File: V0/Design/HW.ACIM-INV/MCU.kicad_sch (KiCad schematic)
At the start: 86 parts, among them J2 ICSP, J5 PSU ICSP, J6 INV DEBUG, J8 ENCODER, Q2 20V/1A, Q3 20V/1A, Q7 20V/1A, SW1 PRG SEL, U11 256Kbit EEPROM, U13 128Mbit Flash, U5 MIPS 32-bit DSC, U6 12MHz (3225), X1 32.768kHz

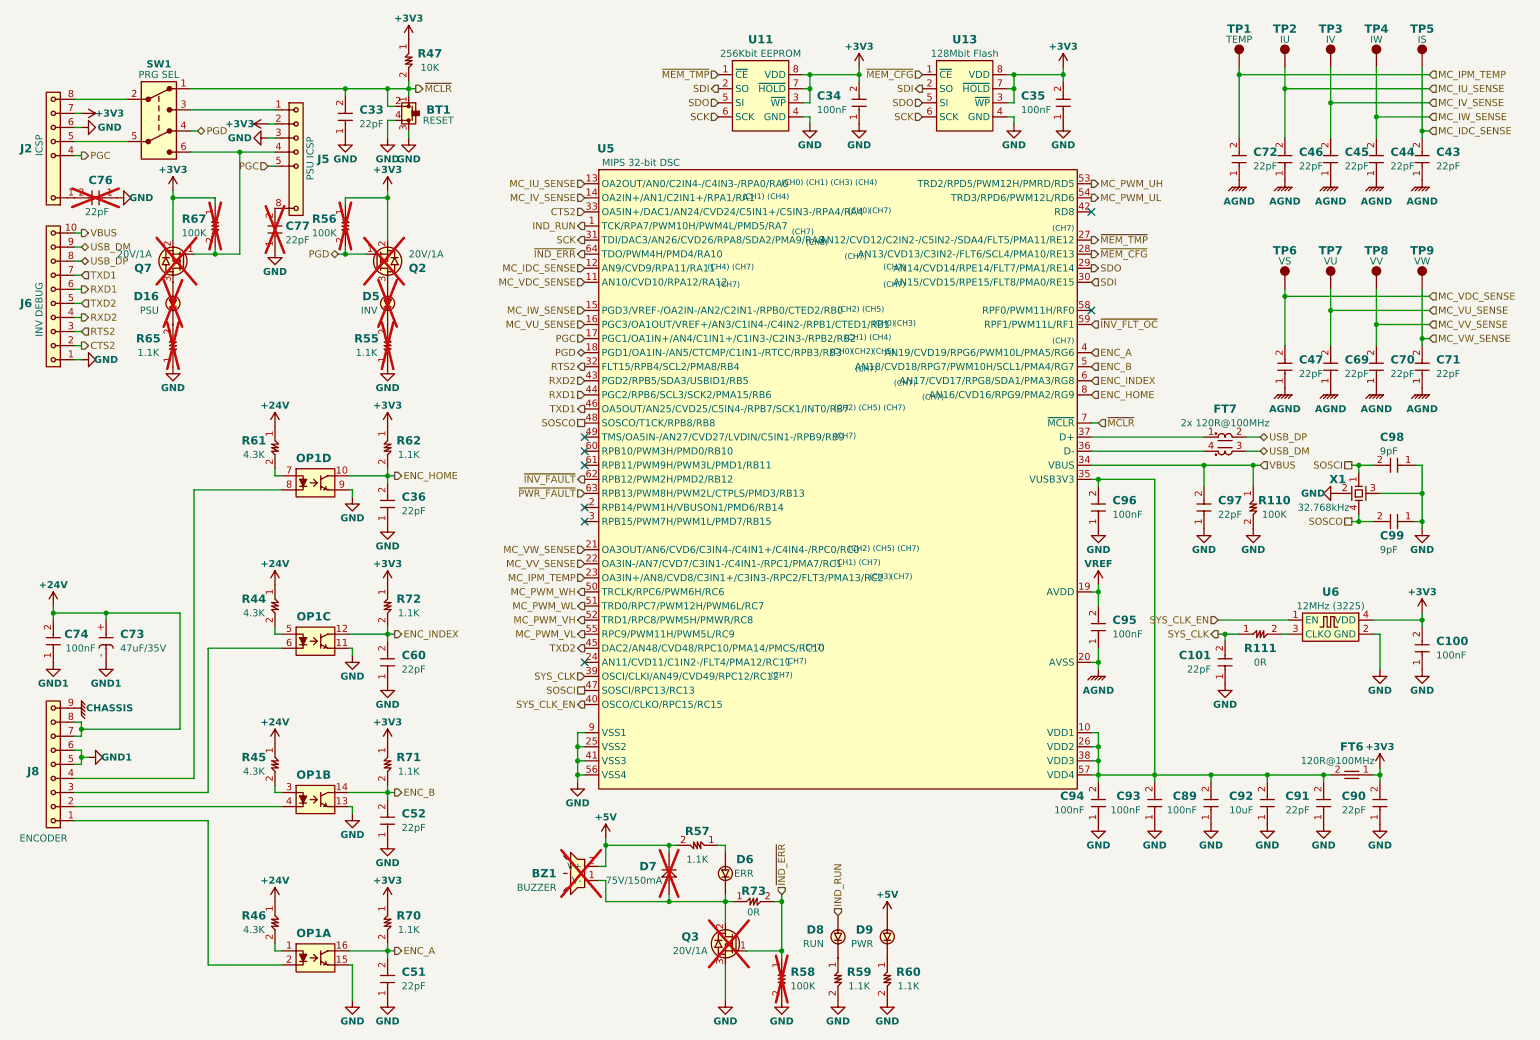
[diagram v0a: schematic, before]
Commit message: HW.ACIM-INV_REV0.0 firmware configuration
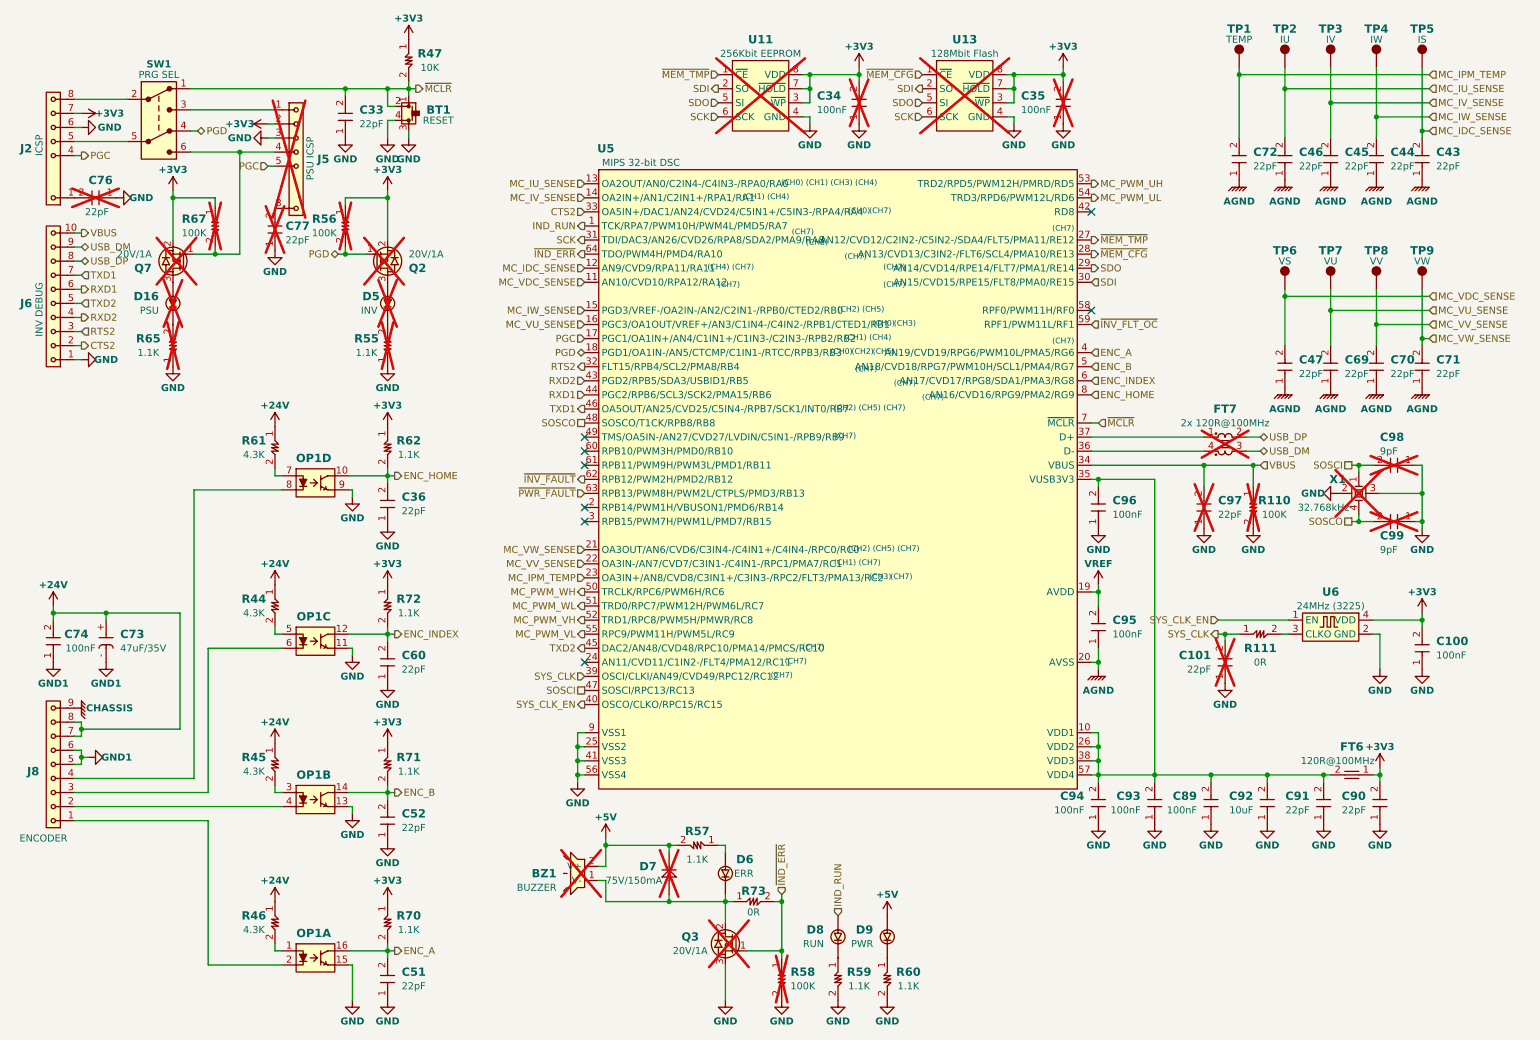
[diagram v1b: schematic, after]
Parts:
- C101, C34, C35, C97, C98, C99, FT7, J5, R110, U11, U13, X1: now not fitted; now left out of the parts list
- U6: value 12MHz (3225) -> 24MHz (3225)
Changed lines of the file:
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@@
 			(justify right)
 		)
-		(property "Netclass" "ADCH0"
+		(property "Netclass" "ADCH3"
 			(at 101.6 44.45 0)
 			(effects
@@
 			(justify right)
 		)
-		(property "Netclass" "ADCH2"
+		(property "Netclass" "ADCH5"
 			(at 101.6 67.31 0)
 			(effects
@@
 			(justify right)
 		)
-		(property "Netclass" "ADCH1"
+		(property "Netclass" "ADCH4"
 			(at 101.6 46.99 0)
 			(effects
@@
 			)
 		)
-		(property "Value" "12MHz (3225)"
+		(property "Value" "24MHz (3225)"
 			(at 250.19 120.65 0)
 			(effects
@@
 		(unit 1)
 		(exclude_from_sim no)
-		(in_bom yes)
+		(in_bom no)
 		(on_board yes)
-		(dnp no)
+		(dnp yes)
 		(property "Reference" "R110"
 			(at 240.03 101.6 90)
@@
 		(unit 1)
 		(exclude_from_sim no)
-		(in_bom yes)
+		(in_bom no)
 		(on_board yes)
-		(dnp no)
+		(dnp yes)
 		(property "Reference" "C35"
 			(at 194.31 28.575 90)
@@
 		(unit 1)
 		(exclude_from_sim no)
-		(in_bom yes)
+		(in_bom no)
 		(on_board yes)
-		(dnp no)
+		(dnp yes)
 		(property "Reference" "U11"
 			(at 147.32 18.415 0)
@@
 		(unit 1)
 		(exclude_from_sim no)
-		(in_bom yes)
+		(in_bom no)
 		(on_board yes)
-		(dnp no)
+		(dnp yes)
 		(property "Reference" "C99"
 			(at 259.08 107.95 0)
@@
 		(unit 1)
 		(exclude_from_sim no)
-		(in_bom yes)
+		(in_bom no)
 		(on_board yes)
-		(dnp no)
+		(dnp yes)
 		(property "Reference" "J5"
 			(at 67.31 40.005 0)
@@
 		(unit 1)
 		(exclude_from_sim no)
-		(in_bom yes)
+		(in_bom no)
 		(on_board yes)
-		(dnp no)
+		(dnp yes)
 		(property "Reference" "X1"
 			(at 251.46 97.79 90)
@@
 		(unit 1)
 		(exclude_from_sim no)
-		(in_bom yes)
+		(in_bom no)
 		(on_board yes)
-		(dnp no)
+		(dnp yes)
 		(property "Reference" "C34"
 			(at 157.48 28.575 90)
@@
 		(unit 1)
 		(exclude_from_sim no)
-		(in_bom yes)
+		(in_bom no)
 		(on_board yes)
-		(dnp no)
+		(dnp yes)
 		(property "Reference" "U13"
 			(at 184.15 18.415 0)
@@
 		(unit 1)
 		(exclude_from_sim no)
-		(in_bom yes)
+		(in_bom no)
 		(on_board yes)
-		(dnp no)
+		(dnp yes)
 		(property "Reference" "C98"
 			(at 259.08 90.17 0)
@@
 		(unit 1)
 		(exclude_from_sim no)
-		(in_bom yes)
+		(in_bom no)
 		(on_board yes)
-		(dnp no)
+		(dnp yes)
 		(fields_autoplaced yes)
 		(property "Reference" "C101"
@@
 		(unit 1)
 		(exclude_from_sim no)
-		(in_bom yes)
+		(in_bom no)
 		(on_board yes)
-		(dnp no)
+		(dnp yes)
 		(property "Reference" "FT7"
 			(at 231.14 85.09 0)
@@
 		(unit 1)
 		(exclude_from_sim no)
-		(in_bom yes)
+		(in_bom no)
 		(on_board yes)
-		(dnp no)
+		(dnp yes)
 		(fields_autoplaced yes)
 		(property "Reference" "C97"
